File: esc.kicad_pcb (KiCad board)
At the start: 2 copper layers, 73 parts, among them J1 Conn_01x02, J2 Screw_Terminal_01x01, J3 Screw_Terminal_01x01, J4 Screw_Terminal_01x01, J5 3220-10-0100-00, Q1 SIR182DP-T1-RE3, Q2 SIR182DP-T1-RE3, Q3 SIR182DP-T1-RE3, Q4 SIR182DP-T1-RE3, Q5 SIR182DP-T1-RE3, Q6 SIR182DP-T1-RE3, SW1 RotaryEncoder, U1 TPS7A20xxxDQN, U2 STM32G484CETx, U3 TPS562201DDCR, U4 TVS0500DRV, U5 IR2103STRPBF, U6 IR2103STRPBF, U7 IR2103STRPBF, Y1 32.768KHz

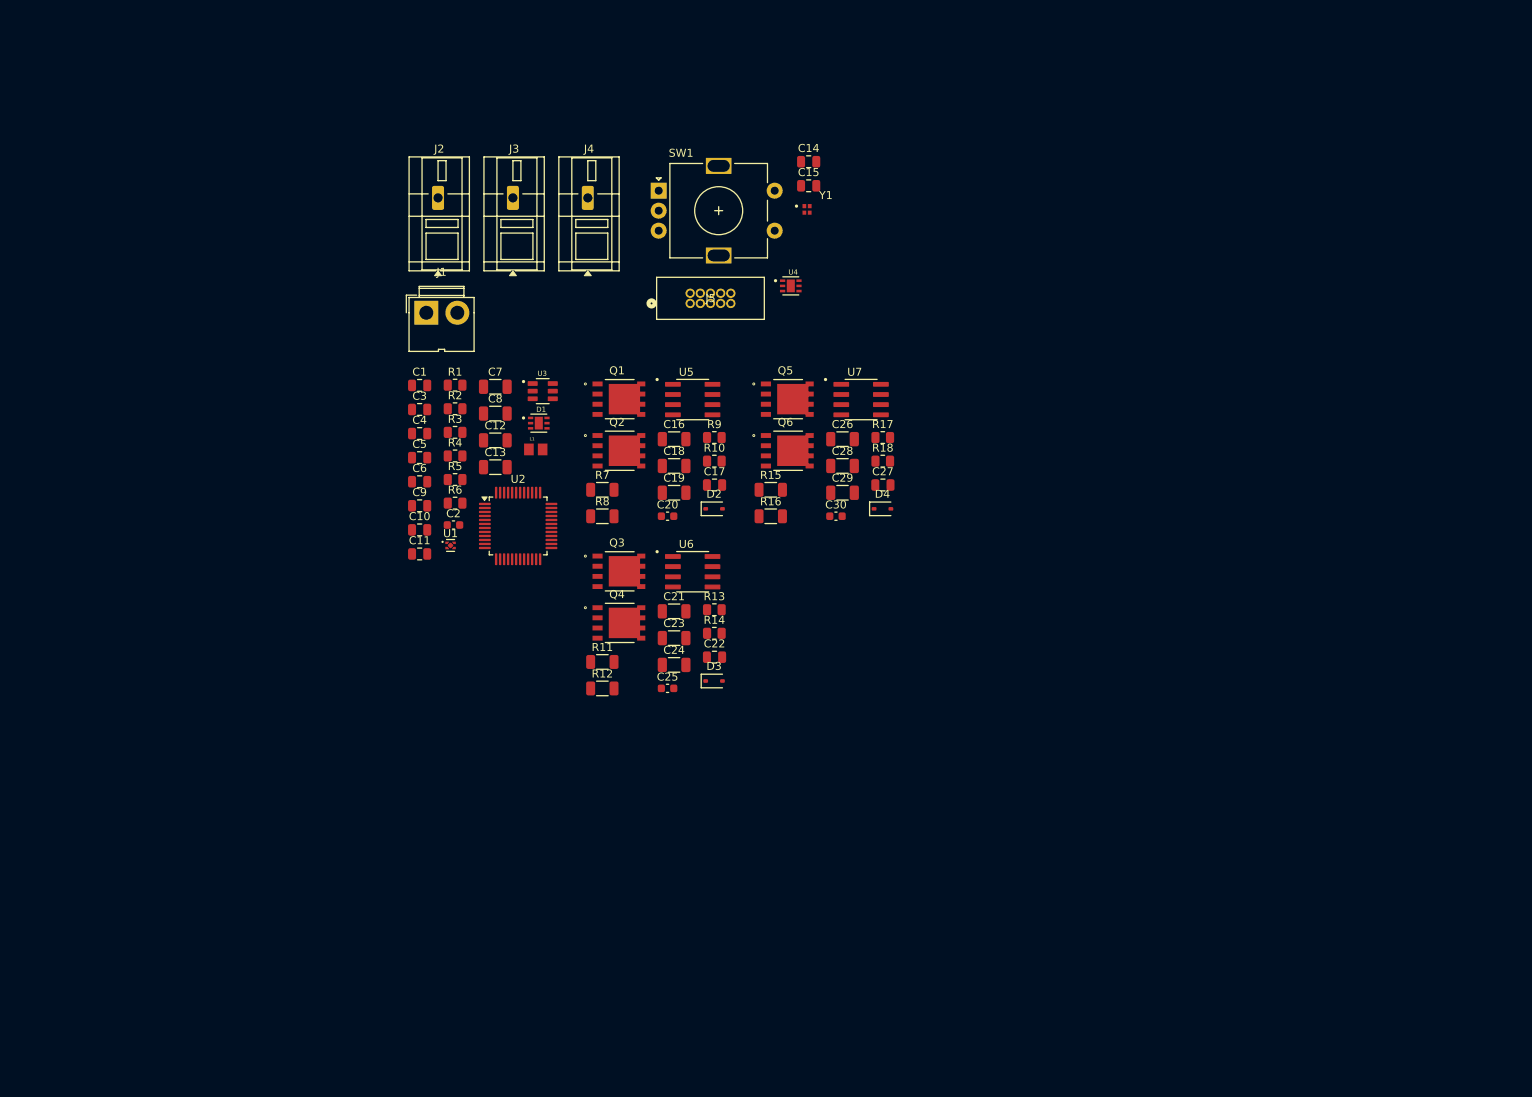
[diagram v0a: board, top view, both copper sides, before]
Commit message: Buck layout; MOSFET layout
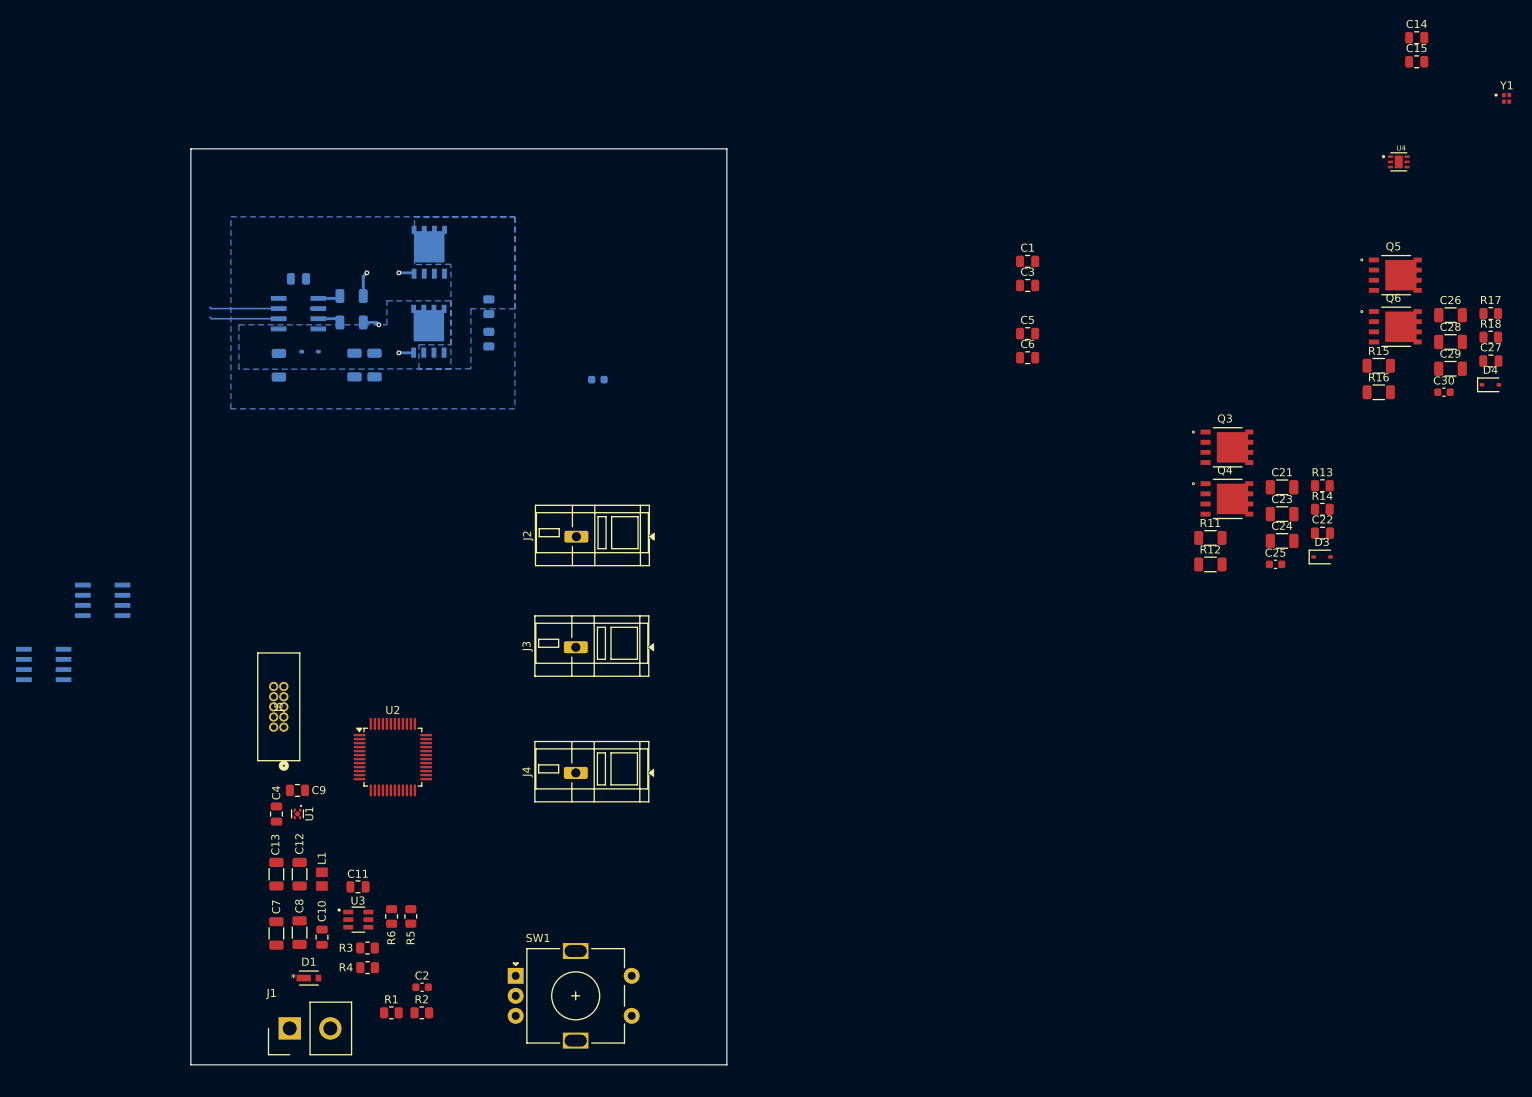
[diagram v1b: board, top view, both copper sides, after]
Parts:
- C16, C17, C18, C19, C20, D2, Q1, Q2, R10, R7, R8, R9, U5, U6, U7: moved to B.Cu
- D1: footprint esc-land-patterns:SON65P200X200X80-7N -> esc-land-patterns:SOD-323HEUS2H_TOS
- J1: footprint Connector:JWT_A3963_1x02_P3.96mm_Vertical -> Connector_Samtec_HPM_THT:Samtec_HPM-02-01-x-S_Straight_1x02_Pitch5.08mm
- moved U7 107.4 mm to (74.1, 125.0)
- moved SW1 99.8 mm to (133.1, 163.9)
- moved J1 91.1 mm to (104.9, 170.4), turned to 90 degrees
- moved Y1 88.5 mm to (257.0, 54.2)
- moved R1 78.9 mm to (117.6, 168.5)
- moved C1 77.6 mm to (197.1, 74.6)
- moved C14 77.6 mm to (245.7, 46.6)
- moved C15 77.6 mm to (245.7, 49.6)
- moved C21 77.6 mm to (228.9, 102.8)
- moved C22 77.6 mm to (234.0, 108.5)
- moved C23 77.6 mm to (228.9, 106.2)
- moved C24 77.6 mm to (228.9, 109.5)
- moved C25 77.6 mm to (228.1, 112.4)
- moved C26 77.6 mm to (250.0, 81.3)
- moved C27 77.6 mm to (255.0, 87.0)
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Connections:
- net Net-(U3-VBST) renamed /PWR/VBST
- net Net-(U3-VFB) renamed /PWR/VFB
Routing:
- net Net-(Q2-Pad4): track 0.00 -> 9.02 mm, vias 0 -> 2
- net /STM32/U_LIN: track 0.00 -> 8.69 mm
- net /STM32/U_HIN: track 0.00 -> 8.69 mm
- net Net-(Q1-Pad4): track 0.00 -> 8.47 mm, vias 0 -> 2
- net Net-(U5-HO): track 0.00 -> 2.89 mm
- net Net-(U5-LO): track 0.00 -> 2.82 mm
- net /U PHASE/U_PHASE: track 0.00 -> 0.98 mm
- added copper zone on B.Cu, net /U PHASE/U_PHASE
- added copper zone on B.Cu, net GND
- added copper zone on B.Cu, net VCC
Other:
- board outline added: 67 x 114.5 mm
- copper layers 2 -> 4

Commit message: MOSFET placement
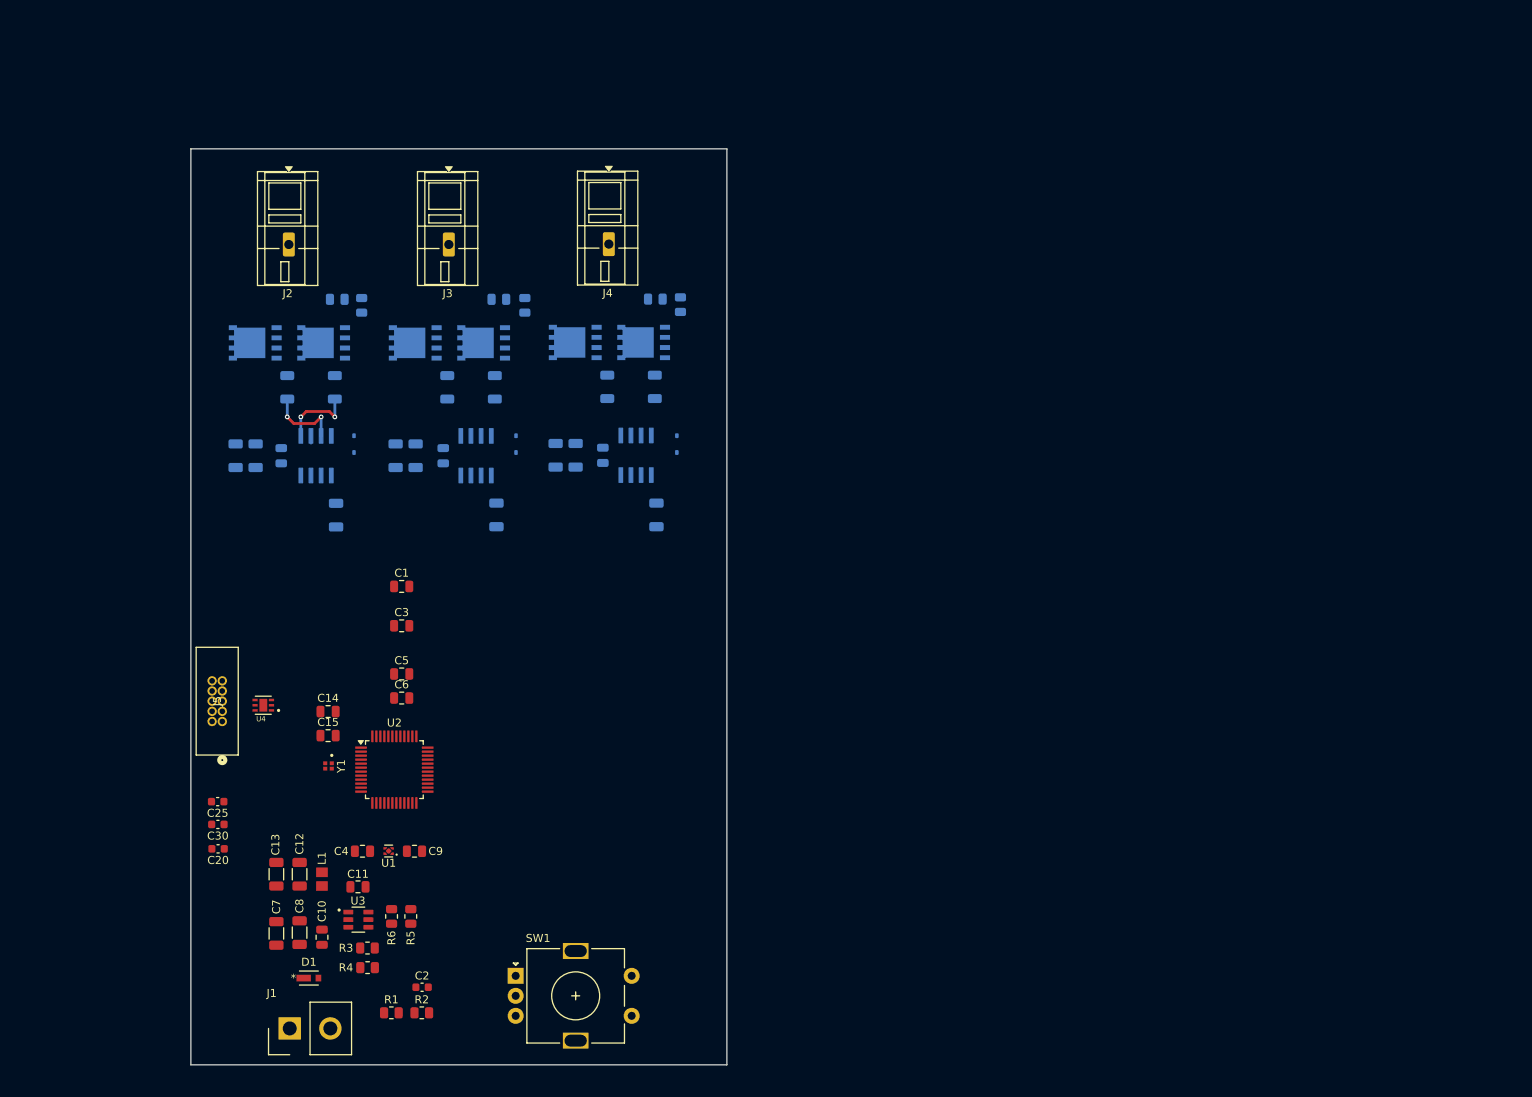
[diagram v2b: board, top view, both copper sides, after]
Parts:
- C20: moved to F.Cu
- C21, C22, C23, C24, C26, C27, C28, C29, D3, D4, Q3, Q4, Q5, Q6, R11, R12, R13, R14, R15, R16, R17, R18: moved to B.Cu
- moved Y1 169.3 mm to (109.7, 137.6), turned to -90 degrees
- moved C30 162.5 mm to (95.9, 144.9), turned to 180 degrees
- moved C14 160.0 mm to (109.7, 130.8)
- moved C15 160.0 mm to (109.7, 133.8)
- moved U4 157.4 mm to (101.5, 130.1), turned to 180 degrees
- moved C25 135.5 mm to (95.8, 142.1), turned to 180 degrees
- moved C28 112.8 mm to (138.1, 98.8), turned to 90 degrees
- moved C27 111.6 mm to (144.0, 98.8), turned to 90 degrees
- moved C23 111.1 mm to (118.1, 98.9), turned to 90 degrees
- moved C22 110.3 mm to (124.0, 98.9), turned to 90 degrees
- moved C29 109.9 mm to (140.6, 98.8), turned to 90 degrees
- moved C24 108.8 mm to (120.6, 98.9), turned to 90 degrees
- moved R13 105.5 mm to (131.0, 79.3)
- moved R17 104.4 mm to (150.6, 79.3), turned to 180 degrees
- moved R14 102.9 mm to (134.2, 80.1), turned to -90 degrees
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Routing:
- net Net-(Q2-Pad4): track 9.02 -> 0.00 mm, vias 2 -> 0
- net /STM32/U_LIN: track 8.69 -> 0.00 mm
- net /STM32/U_HIN: track 8.69 -> 0.00 mm
- net Net-(Q1-Pad4): track 8.47 -> 0.00 mm, vias 2 -> 0
- net Net-(U5-HO): track 2.89 -> 9.53 mm, vias 0 -> 2
- net Net-(U5-LO): track 2.82 -> 9.42 mm, vias 0 -> 2
- removed copper zone on B.Cu, net /U PHASE/U_PHASE
- removed copper zone on B.Cu, net GND
- removed copper zone on B.Cu, net VCC

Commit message: Crystal routing/placement
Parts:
- C14, C15: footprint Capacitor_SMD:C_0805_2012Metric -> Capacitor_SMD:C_0603_1608Metric
- moved C15 5.54 mm to (108.2, 139.2), turned to 90 degrees
- moved C14 5.38 mm to (108.2, 136.0), turned to 90 degrees
- moved Y1 0.93 mm to (110.6, 137.8), turned to 0 degrees
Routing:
- net /STM32/HSE_OUT: track 0.00 -> 6.72 mm
- net /STM32/HSE_IN: track 0.00 -> 6.52 mm
- added copper zone on F.Cu, net GND

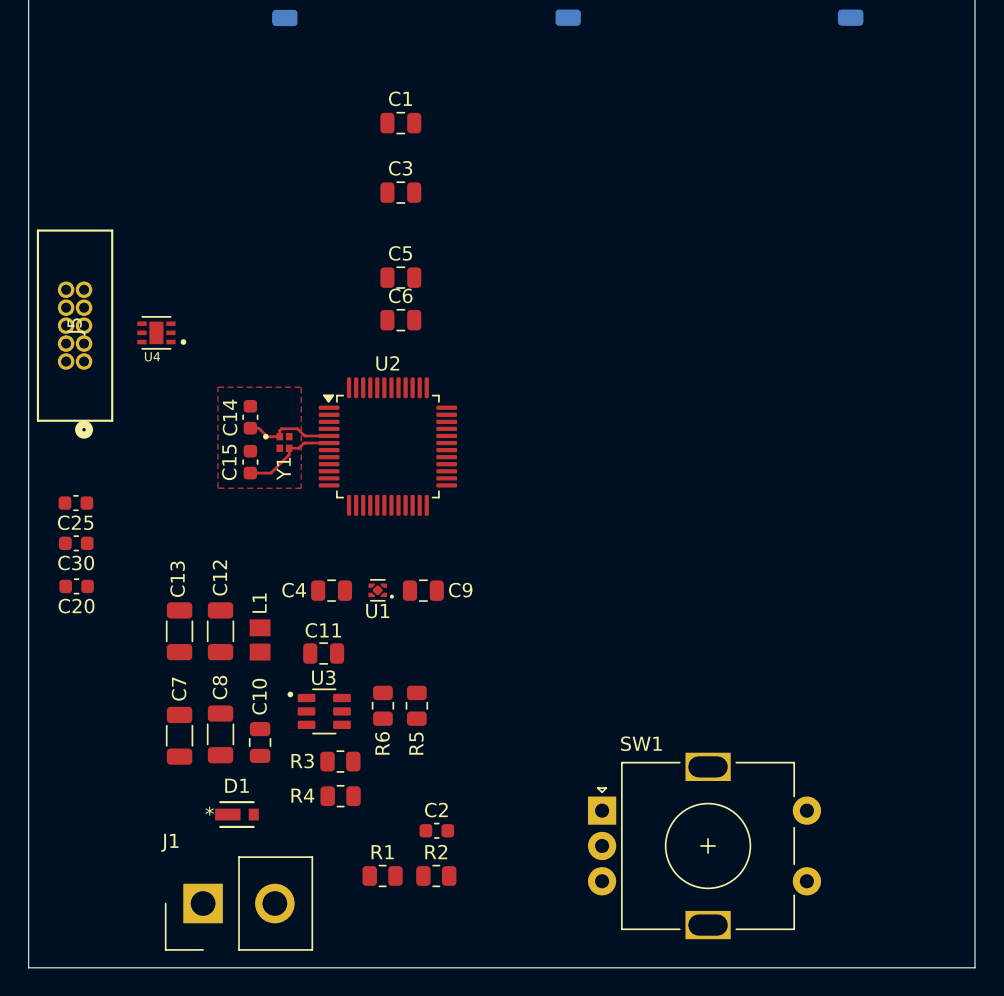
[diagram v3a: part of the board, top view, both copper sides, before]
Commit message: 3V3 and VDDA placement
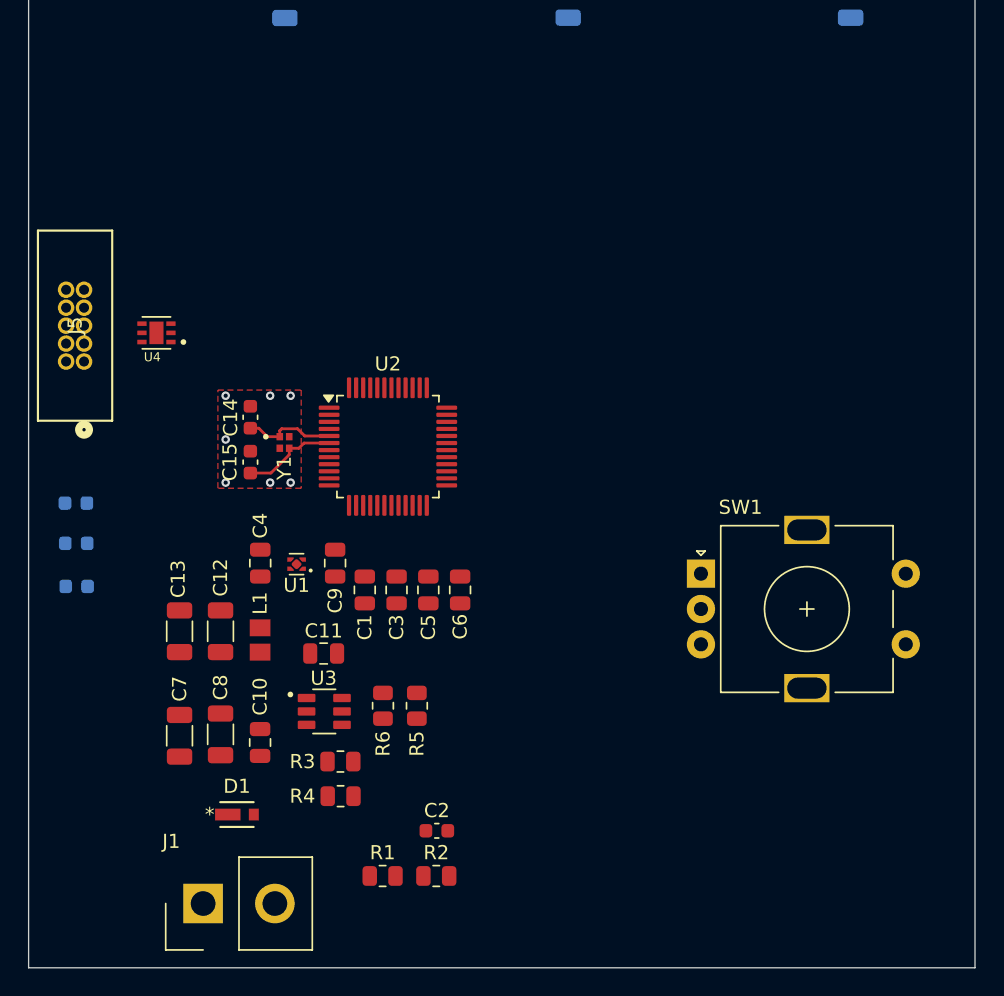
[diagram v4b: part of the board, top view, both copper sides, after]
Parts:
- C20, C25, C30: moved to B.Cu
- moved C1 33.1 mm to (116.3, 148.2), turned to 90 degrees
- moved C3 28.1 mm to (118.5, 148.2), turned to 90 degrees
- moved C5 22.2 mm to (120.8, 148.2), turned to 90 degrees
- moved C6 19.6 mm to (123.0, 148.2), turned to 90 degrees
- moved SW1 18.2 mm to (140.1, 147.1)
- moved C9 6.55 mm to (114.2, 146.3), turned to -90 degrees
- moved U1 6.04 mm to (111.5, 146.4)
- moved C4 5.41 mm to (108.9, 146.3), turned to 90 degrees
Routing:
- net GND: vias 0 -> 7
